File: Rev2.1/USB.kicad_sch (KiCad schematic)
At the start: 32 parts, among them J1 Termination, J10 GPIO, J12 5V power breakout, J2 CAN1, J3 Termination, J4 CAN2, J5 3.3V power breakout, J6 LIN Pots, J7 AIN, U1 STM32F429ZITx, U2 TJA1051T, U3 TJA1051T

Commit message: finished the schematic and footprint assignment
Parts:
- removed C1: 100n, Capacitor_SMD:C_0603_1608Metric_Pad1.08x0.95mm_HandSolder, symbol Device:C_Small
- removed J1, J3: Termination, Connector_PinHeader_2.54mm:PinHeader_1x02_P2.54mm_Vertical, symbol Connector:Conn_01x02_Pin
- removed J10: GPIO, TerminalBlock_Phoenix:TerminalBlock_Phoenix_MKDS-1,5-8_1x08_P5.00mm_Horizontal, symbol Connector:Screw_Terminal_01x08
- removed J12: 5V power breakout, Connector_PinHeader_2.54mm:PinHeader_1x02_P2.54mm_Vertical, symbol Connector:Conn_01x02_Pin
- removed J2: CAN1, TerminalBlock_Phoenix:TerminalBlock_Phoenix_MPT-0,5-2-2.54_1x02_P2.54mm_Horizontal, symbol Connector:Screw_Terminal_01x02
- removed J4: CAN2, TerminalBlock_Phoenix:TerminalBlock_Phoenix_MPT-0,5-2-2.54_1x02_P2.54mm_Horizontal, symbol Connector:Screw_Terminal_01x02
- removed J5: 3.3V power breakout, Connector_PinHeader_2.54mm:PinHeader_1x02_P2.54mm_Vertical, symbol Connector:Conn_01x02_Pin
- removed J6: LIN Pots, TerminalBlock_Phoenix:TerminalBlock_Phoenix_MKDS-1,5-4_1x04_P5.00mm_Horizontal, symbol Connector:Screw_Terminal_01x04
- removed J7: AIN, TerminalBlock_Phoenix:TerminalBlock_Phoenix_MKDS-1,5-4_1x04_P5.00mm_Horizontal, symbol Connector:Screw_Terminal_01x04
- removed R10, R11, R12, R16, R9: 10k, Resistor_SMD:R_0603_1608Metric_Pad0.98x0.95mm_HandSolder, symbol Device:R_Small
- removed R17, R18, R19, R20, R21, R22, R23, R24: 5k6, Resistor_SMD:R_0603_1608Metric_Pad0.98x0.95mm_HandSolder, symbol Device:R_Small
- removed R4, R5: 120, Resistor_SMD:R_0603_1608Metric_Pad0.98x0.95mm_HandSolder, symbol Device:R_Small
- removed U1: STM32F429ZITx, Package_QFP:LQFP-144_20x20mm_P0.5mm, symbol MCU_ST_STM32F4:STM32F429ZITx
- removed U2, U3: TJA1051T, Package_SO:SOIC-8_3.9x4.9mm_P1.27mm, symbol Interface_CAN_LIN:TJA1051T
- removed U5: ~, Package_LGA:LGA-14_3x2.5mm_P0.5mm_LayoutBorder3x4y, symbol custom parts library:LSM6DSOX
- added C23: 100n, Capacitor_SMD:C_0603_1608Metric_Pad1.08x0.95mm_HandSolder, symbol Device:C_Small
- added C24, C25: 6p, Capacitor_SMD:C_0603_1608Metric_Pad1.08x0.95mm_HandSolder, symbol Device:C_Small
- added D2, D3: LED, LED_SMD:LED_0603_1608Metric_Pad1.05x0.95mm_HandSolder, symbol Device:LED
- added J10: Conn_01x08_Pin, Connector_PinHeader_2.54mm:PinHeader_1x08_P2.54mm_Vertical, symbol Connector:Conn_01x08_Pin
- added J8: USB_OTG, Connector_USB:USB_Mini-B_Wuerth_65100516121_Horizontal, symbol Connector:USB_OTG
- added P1: USB_C_Plug_USB2.0, Connector_USB:USB_C_Receptacle_GCT_USB4105-xx-A_16P_TopMnt_Horizontal, symbol Connector:USB_C_Plug_USB2.0
- added R8: 5k1, Resistor_SMD:R_0603_1608Metric_Pad0.98x0.95mm_HandSolder, symbol Device:R_Small
- added U5: MCP2200T-I-SO, Package_SO:SOIC-20W_7.5x12.8mm_P1.27mm, symbol Interface_USB:MCP2200T-I-SO
- added U6: STMPS2151STR(Current protection), Package_TO_SOT_SMD:SOT-23-5_HandSoldering, symbol custom parts library:STMPS2151STR
- added U7 (x2): USBLC6-2P6(ESD protection), Package_TO_SOT_SMD:SOT-666, symbol Power_Protection:USBLC6-2P6
- added Y1: 12MHz, Crystal:Crystal_SMD_3225-4Pin_3.2x2.5mm_HandSoldering, symbol Device:Crystal_GND24
- R13: value 10k -> 4k7; JLCpart# (none) -> C473239
- R14, R15: value 10k -> 2k2; JLCpart# (none) -> C427273
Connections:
- net L1 is gone; now on net +3.3V: R13.2
- net +3.3V: now also C23.1, U5.1 (VDD), U5.17 (V_USB)
- net +5V: now also P1.A4 (VBUS), P1.A9 (VBUS), P1.B4 (VBUS), P1.B9 (VBUS), U6.5 (VIN), U7.5 (VBUS), U7.5 (VBUS)
- net GND: now also R14.1, R15.1, C23.2, C24.2, C25.2, J8.5 (GND), J8.6 (Shield), P1.A1 (GND), P1.A12 (GND), P1.B1 (GND), P1.B12 (GND), P1.S1 (SHIELD), R8.2, U5.20 (VSS), U6.2 (GND), U7.2 (GND), U7.2 (GND), Y1.2, Y1.4
- net STMPS2151STR_EN: now also U6.4 (EN)
- net STMPS2151STR_FAULT: now also U6.3 (FAULT)
- net USART1_RX: now also U5.10 (TX)
- net USART1_TX: now also U5.12 (RX)
- net USB_DATA+: now also U7.6 (I/O1)
- net USB_DATA-: now also U7.4 (I/O2)
- net at R13.1: now also U5.4 (RST)
- net L2: no longer names the net of R14.2
- net L2: now also D2.1 (K)
- net L4: no longer names the net of R15.2
- net L4: now also D3.1 (K)
- new net: P1.A5 (CC), R8.1
- new net: C25.1, U5.3 (OSC2), Y1.1
- new net: C24.1, U5.2 (OSC1), Y1.3
- new net: D3.2 (A), U5.5 (GP7/TxLED)
- new net: D2.2 (A), U5.6 (GP6/RxLED)
- new net CTS: J10.7 (Pin_7), U5.13 (CTS)
- new net GP0: J10.6 (Pin_6), U5.16 (GP0/SSPND)
- new net GP1: J10.5 (Pin_5), U5.15 (GP1/USB-CFG)
- new net GP2: J10.4 (Pin_4), U5.14 (GP2)
- new net GP3: J10.3 (Pin_3), U5.9 (GP3)
- new net GP4: J10.2 (Pin_2), U5.8 (GP4)
- new net GP5: J10.1 (Pin_1), U5.7 (GP5)
- new net RTS: J10.8 (Pin_8), U5.11 (RTS)
- new net USB->ESD+: J8.3 (D+), U7.1 (I/O1)
- new net USB->ESD-: J8.2 (D-), U7.3 (I/O2)
- new net USB->UART+: P1.A7 (D-), U7.1 (I/O1)
- new net USB->UART-: P1.A6 (D+), U7.3 (I/O2)
- new net USB_PROG+: U5.19 (D+), U7.6 (I/O1)
- new net USB_PROG-: U5.18 (D-), U7.4 (I/O2)
- new net VBUS1: J8.1 (VBUS), U6.1 (OUT)
- no-connect marks 71 -> 2
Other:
- removed sheet Ethernet
- removed sheet USB wiring
- removed sheet stm32Basics
- note added: "CX3225GB12000D0HPQCC"
- note added: "Check these USB C connections as I'm not 100% these connections can achieve what is needed"
- note added: "MCP breakout pins"
- note added: "USB Data transfer"
- note removed: "Analog Pin"
- note removed: "GPIO"
- title: rev2.1 -> (none)

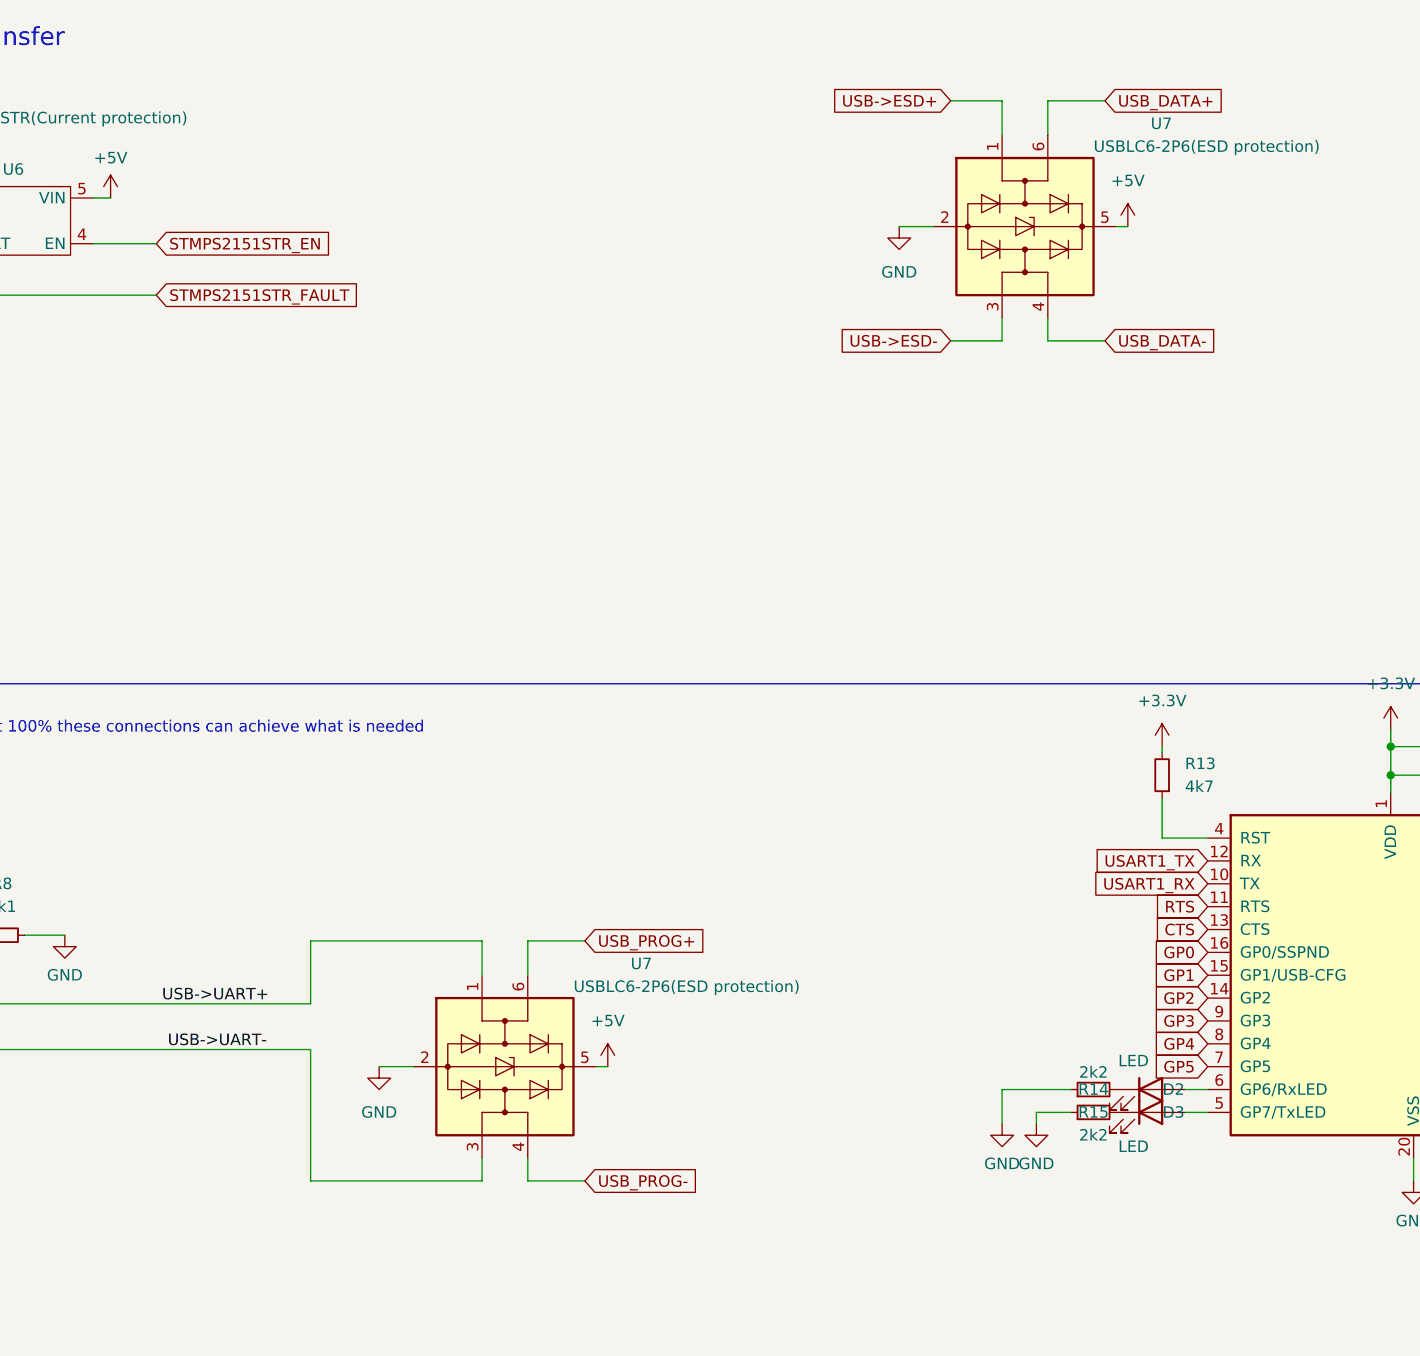
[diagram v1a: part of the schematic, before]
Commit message: added pull up resistors to the I2c Lines for LSM and did mock up placements for PCB
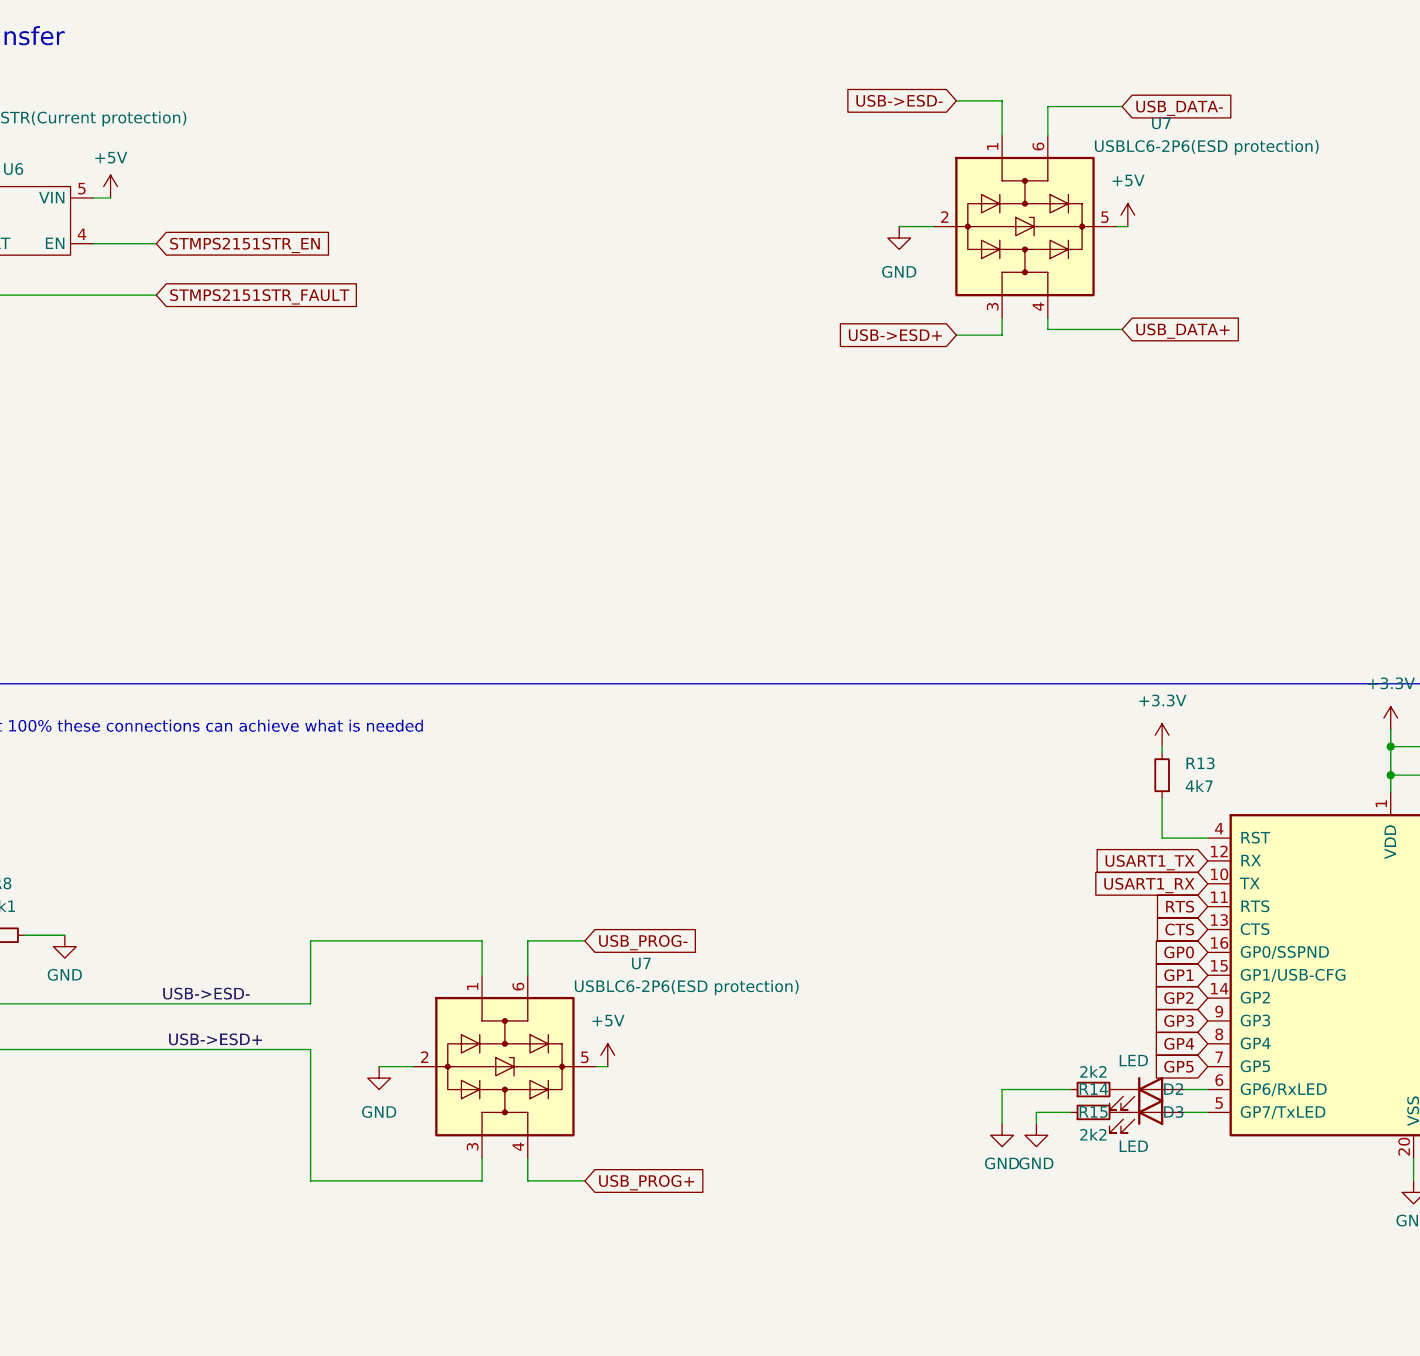
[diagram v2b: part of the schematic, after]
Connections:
- net USB->UART+ is gone; now on net USB->ESD-: P1.A7 (D-), U7.1 (I/O1)
- net USB->UART- is gone; now on net USB->ESD+: P1.A6 (D+), U7.3 (I/O2)
- net USB->ESD+: now also U7.3 (I/O2); no longer U7.1 (I/O1)
- net USB->ESD-: now also U7.1 (I/O1); no longer U7.3 (I/O2)
- net USB_DATA+: now also U7.4 (I/O2); no longer U7.6 (I/O1)
- net USB_DATA-: now also U7.6 (I/O1); no longer U7.4 (I/O2)
- net USB_PROG+: now also U7.4 (I/O2); no longer U7.6 (I/O1)
- net USB_PROG-: now also U7.6 (I/O1); no longer U7.4 (I/O2)
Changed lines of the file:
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@@
     (stroke (width 0) (type default))
   )
-  (wire (pts (xy 180.34 48.895) (xy 180.34 51.435))
-    (stroke (width 0) (type default))
-  )
   (wire (pts (xy 57.15 112.395) (xy 55.245 112.395))
     (stroke (width 0) (type default))
@@
     (stroke (width 0) (type default))
   )
+  (wire (pts (xy 180.34 50.165) (xy 180.34 48.895))
+    (stroke (width 0) (type default))
+  )
   (wire (pts (xy 265.43 146.685) (xy 259.08 146.685))
     (stroke (width 0) (type default))
@@
     (stroke (width 0) (type default))
   )
-  (wire (pts (xy 180.34 28.575) (xy 180.34 24.765))
-    (stroke (width 0) (type default))
-  )
   (wire (pts (xy 218.44 99.695) (xy 218.44 101.6))
     (stroke (width 0) (type default))
@@
     (stroke (width 0) (type default))
   )
-  (wire (pts (xy 180.34 24.765) (xy 186.69 24.765))
-    (stroke (width 0) (type default))
-  )
   (wire (pts (xy 189.23 38.735) (xy 187.96 38.735))
     (stroke (width 0) (type default))
@@
     (stroke (width 0) (type default))
   )
-  (wire (pts (xy 175.26 51.435) (xy 169.545 51.435))
-    (stroke (width 0) (type default))
-  )
   (wire (pts (xy 56.515 35.56) (xy 36.195 35.56))
     (stroke (width 0) (type default))
@@
     (stroke (width 0) (type default))
   )
+  (wire (pts (xy 180.34 25.4) (xy 180.34 28.575))
+    (stroke (width 0) (type default))
+  )
   (wire (pts (xy 81.28 40.64) (xy 74.295 40.64))
     (stroke (width 0) (type default))
@@
     (stroke (width 0) (type default))
   )
+  (wire (pts (xy 175.26 50.8) (xy 175.26 48.895))
+    (stroke (width 0) (type default))
+  )
   (wire (pts (xy 122.555 142.24) (xy 122.555 144.78))
     (stroke (width 0) (type default))
@@
     (stroke (width 0) (type default))
   )
+  (wire (pts (xy 170.18 50.8) (xy 175.26 50.8))
+    (stroke (width 0) (type default))
+  )
   (wire (pts (xy 76.2 35.56) (xy 74.295 35.56))
     (stroke (width 0) (type default))
@@
     (stroke (width 0) (type default))
   )
+  (wire (pts (xy 188.595 50.165) (xy 180.34 50.165))
+    (stroke (width 0) (type default))
+  )
   (wire (pts (xy 250.19 141.605) (xy 250.19 137.16))
     (stroke (width 0) (type default))
@@
     (stroke (width 0) (type default))
   )
-  (wire (pts (xy 175.26 48.895) (xy 175.26 51.435))
-    (stroke (width 0) (type default))
-  )
   (wire (pts (xy 55.245 125.095) (xy 98.425 125.095))
     (stroke (width 0) (type default))
@@
     (stroke (width 0) (type default))
   )
-  (wire (pts (xy 259.08 155.575) (xy 267.335 155.575))
+  (wire (pts (xy 188.595 25.4) (xy 180.34 25.4))
     (stroke (width 0) (type default))
   )
-  (wire (pts (xy 180.34 51.435) (xy 186.69 51.435))
+  (wire (pts (xy 259.08 155.575) (xy 267.335 155.575))
     (stroke (width 0) (type default))
   )
@@
     (stroke (width 0) (type default))
   )
+  (wire (pts (xy 170.18 24.765) (xy 175.26 24.765))
+    (stroke (width 0) (type default))
+  )
   (wire (pts (xy 175.26 24.765) (xy 175.26 28.575))
     (stroke (width 0) (type default))
@@
     (stroke (width 0) (type default))
   )
-  (wire (pts (xy 169.545 24.765) (xy 175.26 24.765))
-    (stroke (width 0) (type default))
-  )
   (image (at 48.26 81.28) (scale 0.0494823)
     (data
@@
     (effects (font (size 2 2)) (justify left bottom))
   )
-  (label "USB->UART-" (at 82.55 130.175 0) (fields_autoplaced)
+  (label "USB->ESD+" (at 82.55 130.175 0) (fields_autoplaced)
     (effects (font (size 1.27 1.27)) (justify left bottom))
   )
-  (label "USB->UART+" (at 81.915 125.095 0) (fields_autoplaced)
+  (label "USB->ESD-" (at 81.915 125.095 0) (fields_autoplaced)
     (effects (font (size 1.27 1.27)) (justify left bottom))
   )
@@
     (effects (font (size 1.27 1.27)) (justify left bottom))
   )
-  (global_label "USB->ESD+" (shape input) (at 169.545 24.765 180) (fields_autoplaced)
+  (global_label "USB->ESD+" (shape input) (at 170.18 50.8 180) (fields_autoplaced)
     (effects (font (size 1.27 1.27)) (justify right))
-    (property "Intersheetrefs" "${INTERSHEET_REFS}" (at 154.4041 24.765 0)
+    (property "Intersheetrefs" "${INTERSHEET_REFS}" (at 155.0391 50.8 0)
       (effects (font (size 1.27 1.27)) (justify right) hide)
     )
   )
-  (global_label "USB_PROG-" (shape input) (at 128.905 144.78 0) (fields_autoplaced)
+  (global_label "USB_PROG+" (shape input) (at 128.905 144.78 0) (fields_autoplaced)
     (effects (font (size 1.27 1.27)) (justify left))
     (property "Intersheetrefs" "${INTERSHEET_REFS}" (at 143.3807 144.78 0)
@@
     )
   )
-  (global_label "USB_DATA-" (shape input) (at 186.69 51.435 0) (fields_autoplaced)
+  (global_label "USB_DATA-" (shape input) (at 188.595 25.4 0) (fields_autoplaced)
     (effects (font (size 1.27 1.27)) (justify left))
-    (property "Intersheetrefs" "${INTERSHEET_REFS}" (at 200.44 51.435 0)
+    (property "Intersheetrefs" "${INTERSHEET_REFS}" (at 202.345 25.4 0)
       (effects (font (size 1.27 1.27)) (justify left) hide)
     )
@@
     )
   )
-  (global_label "USB->ESD-" (shape input) (at 169.545 51.435 180) (fields_autoplaced)
+  (global_label "USB->ESD-" (shape input) (at 170.18 24.765 180) (fields_autoplaced)
     (effects (font (size 1.27 1.27)) (justify right))
-    (property "Intersheetrefs" "${INTERSHEET_REFS}" (at 154.4041 51.435 0)
+    (property "Intersheetrefs" "${INTERSHEET_REFS}" (at 155.0391 24.765 0)
       (effects (font (size 1.27 1.27)) (justify right) hide)
     )
@@
     )
   )
-  (global_label "USB_PROG+" (shape input) (at 128.905 118.11 0) (fields_autoplaced)
+  (global_label "USB_PROG-" (shape input) (at 128.905 118.11 0) (fields_autoplaced)
     (effects (font (size 1.27 1.27)) (justify left))
     (property "Intersheetrefs" "${INTERSHEET_REFS}" (at 143.3807 118.11 0)
@@
     )
   )
-  (global_label "USB_DATA+" (shape input) (at 186.69 24.765 0) (fields_autoplaced)
+  (global_label "USB_DATA+" (shape input) (at 188.595 50.165 0) (fields_autoplaced)
     (effects (font (size 1.27 1.27)) (justify left))
-    (property "Intersheetrefs" "${INTERSHEET_REFS}" (at 200.44 24.765 0)
+    (property "Intersheetrefs" "${INTERSHEET_REFS}" (at 202.345 50.165 0)
       (effects (font (size 1.27 1.27)) (justify left) hide)
     )
